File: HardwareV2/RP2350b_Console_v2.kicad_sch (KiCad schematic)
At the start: 0 parts

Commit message: added updated battery and power schematic
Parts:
- added U1: RP2350B_C42415655, parts_lib:QFN-80_L10.0-W10.0-P0.40-TL-EP3.4, symbol RP2350b_part_sch:RP2350B_C42415655
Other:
- added sheet Power_and_Battery_Managment (power.kicad_sch)
- added sheet USB (usb.kicad_sch)

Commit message: commiting before flight :), added in crystal and started doing the labels for the RP2350b
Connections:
- net QSPI_3: now reaches U1.70 (QSPI_SD3)
- net QSPI_CLK: now reaches U1.71 (QSPI_SCLK)
- net QSPI_0: now reaches U1.72 (QSPI_SD0)
- net QSPI_2: now reaches U1.73 (QSPI_SD2)
- net QSPI_1: now reaches U1.74 (QSPI_SD1)
- net QSPI_SS0: now reaches U1.75 (QSPI_SS)
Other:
- added sheet Crystal Oscillator (crystal.kicad_sch)
- added sheet Memory (memory.kicad_sch)

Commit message: updates pre routing
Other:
- added sheet Core (core.kicad_sch)
- added sheet User_IO (user_io.kicad_sch)
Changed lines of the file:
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@@
+	)
+	(sheet
+		(at 173.355 76.2)
+		(size 30.48 32.385)
+		(exclude_from_sim no)
+		(in_bom yes)
+		(on_board yes)
+		(dnp no)
+		(fields_autoplaced yes)
+		(stroke
+			(width 0.1524)
+			(type solid)
+		)
+		(fill
+			(color 0 0 0 0.0000)
+		)
+		(property "Sheetname" "User_IO"
+			(at 173.355 75.4884 0)
+			(effects
+				(font
+					(size 1.27 1.27)
+				)
+				(justify left bottom)
+			)
+		)
+		(property "Sheetfile" "user_io.kicad_sch"
+			(at 173.355 109.1696 0)
+			(effects
+				(font
+					(size 1.27 1.27)
+				)
+				(justify left top)
+			)
+		)
+		(instances
+			(project "RP2350b_Console_v2"
+				(path "/72e8720b-5adf-4b6d-9b96-dda4c7035d94"
+					(page "6")
+				)
+			)
+		)
 	)
 	(sheet
@@
 				)
 			)
+		)
+	)
+	(sheet
+		(at 212.09 115.57)
+		(size 31.75 21.59)
+		(exclude_from_sim no)
+		(in_bom yes)
+		(on_board yes)
+		(dnp no)
+		(fields_autoplaced yes)
+		(stroke
+			(width 0.1524)
+			(type solid)
+		)
+		(fill
+			(color 0 0 0 0.0000)
+		)
+		(property "Sheetname" "Core"
+			(at 212.09 114.8584 0)
+			(effects
+				(font
+					(size 1.27 1.27)
+				)
+				(justify left bottom)
+			)
+		)
+		(property "Sheetfile" "core.kicad_sch"
+			(at 212.09 137.7446 0)
+			(effects
+				(font
+					(size 1.27 1.27)
+				)
+				(justify left top)
+			)
+		)
+		(instances
+			(project "RP2350b_Console_v2"
+				(path "/72e8720b-5adf-4b6d-9b96-dda4c7035d94"
+					(page "7")
+				)
+			)

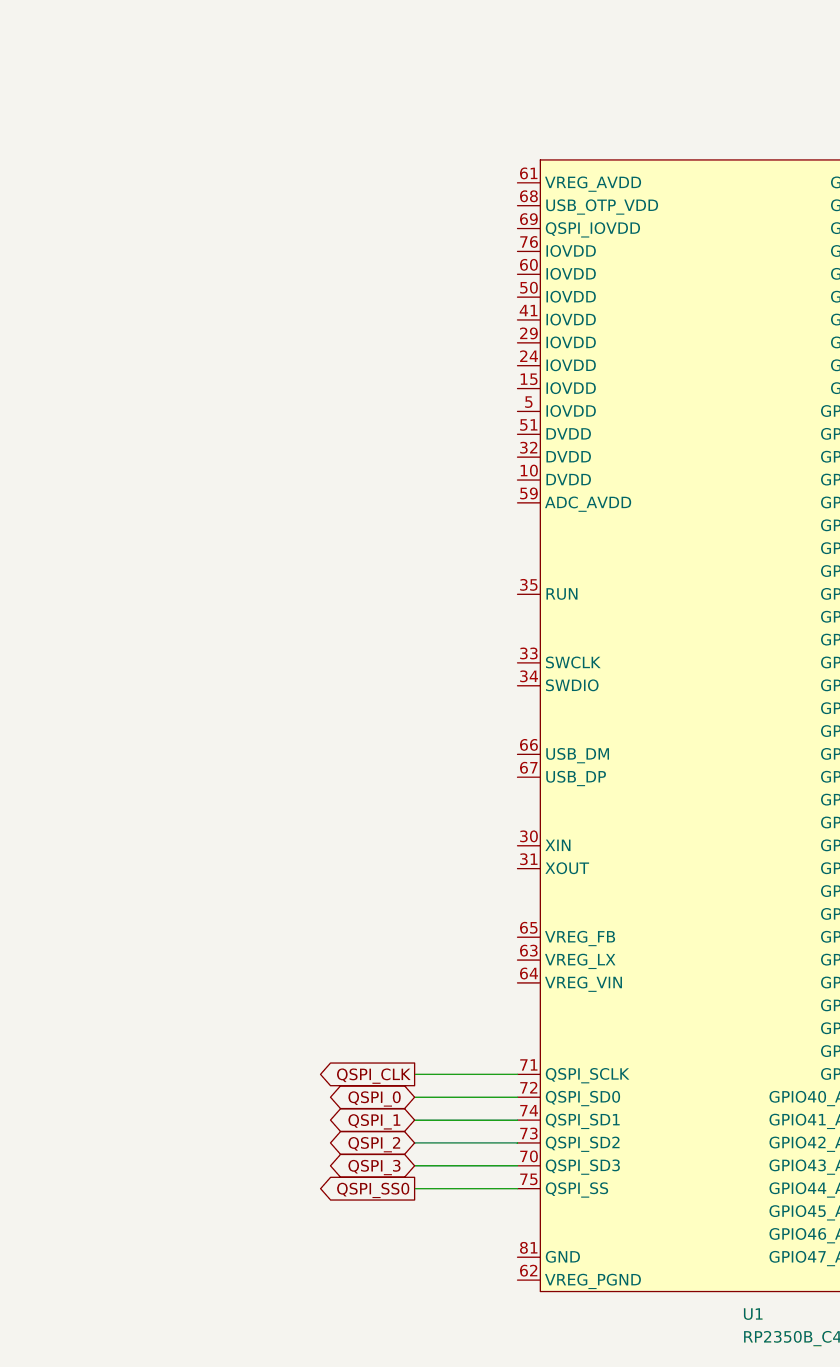
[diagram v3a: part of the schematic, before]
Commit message: initial v2 pcb layout minus passives
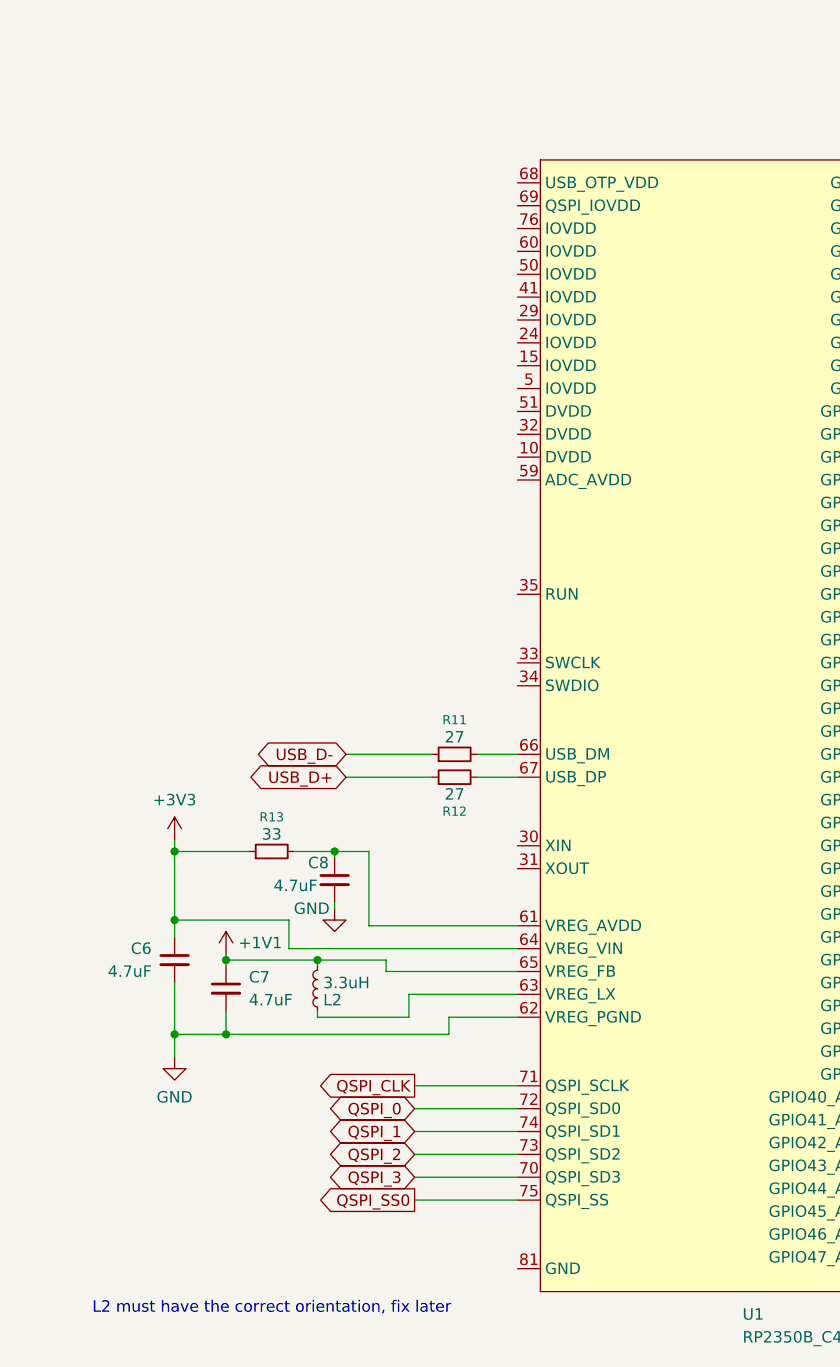
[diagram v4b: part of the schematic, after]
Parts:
- added C6, C7, C8: 4.7uF, symbol Device:C_Small
- added L2: 3.3uH, RP2350b_parts_layout:IND-SMD_L2.0-W1.6_AOTA-B201610S3R3-101-T, symbol Device:L_Small
- added R11, R12: 27, Resistor_SMD:R_0805_2012Metric, symbol Device:R_Small
- added R13: 33, symbol Device:R_Small
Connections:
- net at U1.61 (VREG_AVDD): now also C8.1, R13.2
- net GND: now reaches U1.62 (VREG_PGND)
- net GND: now also C6.2, C7.2, C8.2
- net at U1.63 (VREG_LX): now also L2.1
- net +3V3: now reaches U1.64 (VREG_VIN)
- net +3V3: now also C6.1, R13.1
- net +1V1: now reaches U1.65 (VREG_FB)
- net +1V1: now also C7.1, L2.2
- net at U1.66 (USB_DM): now also R11.2
- net at U1.67 (USB_DP): now also R12.2
- new net USB_D+: R12.1
- new net USB_D-: R11.1
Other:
- note added: "L2 must have the correct orientation, fix later"
